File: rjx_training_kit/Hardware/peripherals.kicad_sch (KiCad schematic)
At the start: 72 parts, among them J4 LiPo_4.2V, J5 LiPo_4.2V, J6 CHG_OUT, J7 CAN_Bus, J8 CAN_Bus, Q2 BC817, Q3 BC817, Q4 BC808, Q5 BC817, SW1 SW_Push, U3 BQ24072RGT, U4 LIS3DH, U5 BQ27441-G1, U6 KCSA02-136, U7 TMP1075DGK, U8 MCP2562-E-SN

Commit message: [RJX]: Initial footprint assignment. This is subject to further review and analysis.
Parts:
- BZ1: footprint (none) -> Buzzer_Beeper:Buzzer_12x9.5RM7.6
- C10, C11, C12, C13, C14, C5, C6, C7, C8, C9: footprint (none) -> Capacitor_SMD:C_0603_1608Metric
- D2, D3, D4, D5: footprint (none) -> LED_SMD:LED_0603_1608Metric
- J4, J5: footprint (none) -> Connector_JST:JST_PH_B2B-PH-K_1x02_P2.00mm_Vertical
- J6, J7, J8, JP1, JP2, JP3, JP4: footprint (none) -> Connector_PinHeader_2.54mm:PinHeader_1x02_P2.54mm_Vertical
- R10, R11, R12, R14, R15, R16, R17, R19, R20, R21, R22, R23, R24, R25, R26, R27, R28, R29, R30, R31, R32, R33, R34, R35, R36, R37, R38, R39, R40, R6, R7, R8, R9: footprint (none) -> Resistor_SMD:R_0603_1608Metric
- R13, R18: footprint (none) -> Resistor_SMD:R_2512_6332Metric
- RV1: footprint (none) -> Potentiometer_THT:Potentiometer_Bourns_3296W_Vertical
- SW1: footprint (none) -> Button_Switch_THT:SW_PUSH_6mm
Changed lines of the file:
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@@
 			)
 		)
-		(property "Footprint" ""
+		(property "Footprint" "Resistor_SMD:R_0603_1608Metric"
 			(at 143.764 152.654 90)
 			(effects
@@
 			)
 		)
-		(property "Footprint" ""
+		(property "Footprint" "Capacitor_SMD:C_0603_1608Metric"
 			(at 186.9948 138.43 0)
 			(effects
@@
 			)
 		)
-		(property "Footprint" ""
+		(property "Footprint" "Resistor_SMD:R_0603_1608Metric"
 			(at 39.116 118.364 90)
 			(effects
@@
 			)
 		)
-		(property "Footprint" ""
+		(property "Footprint" "Resistor_SMD:R_0603_1608Metric"
 			(at 138.684 188.214 90)
 			(effects
@@
 			)
 		)
-		(property "Footprint" ""
+		(property "Footprint" "Connector_PinHeader_2.54mm:PinHeader_1x02_P2.54mm_Vertical"
 			(at 248.92 123.19 0)
 			(effects
@@
 			)
 		)
-		(property "Footprint" ""
+		(property "Footprint" "Resistor_SMD:R_0603_1608Metric"
 			(at 209.296 78.994 90)
 			(effects
@@
 			)
 		)
-		(property "Footprint" ""
+		(property "Footprint" "Resistor_SMD:R_0603_1608Metric"
 			(at 216.154 70.104 90)
 			(effects
@@
 			)
 		)
-		(property "Footprint" ""
+		(property "Footprint" "Capacitor_SMD:C_0603_1608Metric"
 			(at 148.2852 85.09 0)
 			(effects
@@
 			)
 		)
-		(property "Footprint" ""
+		(property "Footprint" "Resistor_SMD:R_0603_1608Metric"
 			(at 230.124 157.734 90)
 			(effects
@@
 			)
 		)
-		(property "Footprint" ""
+		(property "Footprint" "Capacitor_SMD:C_0603_1608Metric"
 			(at 103.8352 153.67 0)
 			(effects
@@
 			)
 		)
-		(property "Footprint" ""
+		(property "Footprint" "Resistor_SMD:R_0603_1608Metric"
 			(at 101.854 76.454 90)
 			(effects
@@
 			)
 		)
-		(property "Footprint" ""
+		(property "Footprint" "Resistor_SMD:R_0603_1608Metric"
 			(at 138.684 175.514 90)
 			(effects
@@
 			)
 		)
-		(property "Footprint" ""
+		(property "Footprint" "Resistor_SMD:R_0603_1608Metric"
 			(at 195.834 33.274 90)
 			(effects
@@
 			)
 		)
-		(property "Footprint" ""
+		(property "Footprint" "Resistor_SMD:R_0603_1608Metric"
 			(at 151.384 157.734 90)
 			(effects
@@
 			)
 		)
-		(property "Footprint" ""
+		(property "Footprint" "Capacitor_SMD:C_0603_1608Metric"
 			(at 126.6952 44.45 0)
 			(effects
@@
 			)
 		)
-		(property "Footprint" ""
+		(property "Footprint" "Resistor_SMD:R_0603_1608Metric"
 			(at 28.194 164.084 90)
 			(effects
@@
 			)
 		)
-		(property "Footprint" ""
+		(property "Footprint" "Connector_PinHeader_2.54mm:PinHeader_1x02_P2.54mm_Vertical"
 			(at 259.08 123.19 0)
 			(effects
@@
 			)
 		)
-		(property "Footprint" ""
+		(property "Footprint" "Resistor_SMD:R_0603_1608Metric"
 			(at 205.486 33.274 90)
 			(effects
@@
 			)
 		)
-		(property "Footprint" ""
+		(property "Footprint" "Connector_PinHeader_2.54mm:PinHeader_1x02_P2.54mm_Vertical"
 			(at 20.32 81.28 0)
 			(effects
@@
 			)
 		)
-		(property "Footprint" ""
+		(property "Footprint" "Resistor_SMD:R_0603_1608Metric"
 			(at 230.886 48.006 90)
 			(effects
@@
 			)
 		)
-		(property "Footprint" ""
+		(property "Footprint" "LED_SMD:LED_0603_1608Metric"
 			(at 200.66 44.45 0)
 			(effects
@@
 			)
 		)
-		(property "Footprint" ""
+		(property "Footprint" "Connector_JST:JST_PH_B2B-PH-K_1x02_P2.00mm_Vertical"
 			(at 34.29 39.37 0)
 			(effects
@@
 			)
 		)
-		(property "Footprint" ""
+		(property "Footprint" "Capacitor_SMD:C_0603_1608Metric"
 			(at 83.5152 87.63 0)
 			(effects
@@
 			)
 		)
-		(property "Footprint" ""
+		(property "Footprint" "Resistor_SMD:R_0603_1608Metric"
 			(at 138.684 180.594 90)
 			(effects
@@
 			)
 		)
-		(property "Footprint" ""
+		(property "Footprint" "Potentiometer_THT:Potentiometer_Bourns_3296W_Vertical"
 			(at 240.03 46.99 0)
 			(effects
@@
 			)
 		)
-		(property "Footprint" ""
+		(property "Footprint" "Resistor_SMD:R_0603_1608Metric"
 			(at 138.684 172.974 90)
 			(effects
@@
 			)
 		)
-		(property "Footprint" ""
+		(property "Footprint" "Resistor_SMD:R_2512_6332Metric"
 			(at 119.634 101.854 90)
 			(effects
@@
 			)
 		)
-		(property "Footprint" ""
+		(property "Footprint" "Capacitor_SMD:C_0603_1608Metric"
 			(at 186.9948 111.76 0)
 			(effects
@@
 			)
 		)
-		(property "Footprint" ""
+		(property "Footprint" "Resistor_SMD:R_2512_6332Metric"
 			(at 91.694 100.584 90)
 			(effects
@@
 			)
 		)
-		(property "Footprint" ""
+		(property "Footprint" "Resistor_SMD:R_0603_1608Metric"
 			(at 30.226 118.364 90)
 			(effects
@@
 			)
 		)
-		(property "Footprint" ""
+		(property "Footprint" "Resistor_SMD:R_0603_1608Metric"
 			(at 138.684 185.674 90)
 			(effects
@@
 			)
 		)
-		(property "Footprint" ""
+		(property "Footprint" "Resistor_SMD:R_0603_1608Metric"
 			(at 61.976 35.814 90)
 			(effects
@@
 			)
 		)
-		(property "Footprint" ""
+		(property "Footprint" "Capacitor_SMD:C_0603_1608Metric"
 			(at 115.2652 153.67 0)
 			(effects
@@
 			)
 		)
-		(property "Footprint" ""
+		(property "Footprint" "Connector_PinHeader_2.54mm:PinHeader_1x02_P2.54mm_Vertical"
 			(at 154.94 140.97 0)
 			(effects
@@
 			)
 		)
-		(property "Footprint" ""
+		(property "Footprint" "Resistor_SMD:R_0603_1608Metric"
 			(at 138.684 183.134 90)
 			(effects
@@
 			)
 		)
-		(property "Footprint" ""
+		(property "Footprint" "Resistor_SMD:R_0603_1608Metric"
 			(at 227.076 131.064 90)
 			(effects
@@
 			)
 		)
-		(property "Footprint" ""
+		(property "Footprint" "Resistor_SMD:R_0603_1608Metric"
 			(at 21.336 118.364 90)
 			(effects
@@
 			)
 		)
-		(property "Footprint" ""
+		(property "Footprint" "Resistor_SMD:R_0603_1608Metric"
 			(at 75.946 115.824 90)
 			(effects
@@
 			)
 		)
-		(property "Footprint" ""
+		(property "Footprint" "Connector_PinHeader_2.54mm:PinHeader_1x02_P2.54mm_Vertical"
 			(at 240.03 31.75 0)
 			(effects
@@
 			)
 		)
-		(property "Footprint" ""
+		(property "Footprint" "Resistor_SMD:R_0603_1608Metric"
 			(at 99.314 115.824 90)
 			(effects
@@
 			)
 		)
-		(property "Footprint" ""
+		(property "Footprint" "Resistor_SMD:R_0603_1608Metric"
 			(at 127.254 92.964 90)
 			(effects
@@
 			)
 		)
-		(property "Footprint" ""
+		(property "Footprint" "LED_SMD:LED_0603_1608Metric"
 			(at 111.76 85.09 0)
 			(effects
@@
 			)
 		)
-		(property "Footprint" ""
+		(property "Footprint" "Buzzer_Beeper:Buzzer_12x9.5RM7.6"
 			(at 45.085 152.4 90)
 			(effects
@@
 			)
 		)
-		(property "Footprint" ""
+		(property "Footprint" "Capacitor_SMD:C_0603_1608Metric"
 			(at 74.6252 43.18 0)
 			(effects
@@
 			)
 		)
-		(property "Footprint" ""
+		(property "Footprint" "Capacitor_SMD:C_0603_1608Metric"
 			(at 83.5152 116.84 0)
 			(effects
@@
 			)
 		)
-		(property "Footprint" ""
+		(property "Footprint" "Resistor_SMD:R_0603_1608Metric"
 			(at 138.176 40.894 90)
 			(effects
@@
 			)
 		)
-		(property "Footprint" ""
+		(property "Footprint" "LED_SMD:LED_0603_1608Metric"
 			(at 133.35 101.6 0)
 			(effects
@@
 			)
 		)
-		(property "Footprint" ""
+		(property "Footprint" "Resistor_SMD:R_0603_1608Metric"
 			(at 108.204 115.824 90)
 			(effects
@@
 			)
 		)
-		(property "Footprint" ""
+		(property "Footprint" "Resistor_SMD:R_0603_1608Metric"
 			(at 138.684 190.754 90)
 			(effects
@@
 			)
 		)
-		(property "Footprint" ""
+		(property "Footprint" "Button_Switch_THT:SW_PUSH_6mm"
 			(at 157.48 43.18 0)
 			(effects
@@
 			)
 		)
-		(property "Footprint" ""
+		(property "Footprint" "Resistor_SMD:R_0603_1608Metric"
 			(at 230.124 162.814 90)
 			(effects
@@
 			)
 		)
-		(property "Footprint" ""
+		(property "Footprint" "Capacitor_SMD:C_0603_1608Metric"
 			(at 21.2852 96.52 0)
 			(effects
@@
 			)
 		)
-		(property "Footprint" ""
+		(property "Footprint" "Resistor_SMD:R_0603_1608Metric"
 			(at 230.124 160.274 90)
 			(effects
@@
 			)
 		)
-		(property "Footprint" ""
+		(property "Footprint" "Resistor_SMD:R_0603_1608Metric"
 			(at 61.976 45.974 90)
 			(effects
@@
 			)
 		)
-		(property "Footprint" ""
+		(property "Footprint" "Resistor_SMD:R_0603_1608Metric"
 			(at 101.854 84.074 90)
 			(effects
@@
 			)
 		)
-		(property "Footprint" ""
+		(property "Footprint" "Connector_PinHeader_2.54mm:PinHeader_1x02_P2.54mm_Vertical"
 			(at 226.06 119.38 0)
 			(effects
@@
 			)
 		)
-		(property "Footprint" ""
+		(property "Footprint" "LED_SMD:LED_0603_1608Metric"
 			(at 111.76 77.47 0)
 			(effects
@@
 			)
 		)
-		(property "Footprint" ""
+		(property "Footprint" "Connector_PinHeader_2.54mm:PinHeader_1x02_P2.54mm_Vertical"
 			(at 45.72 36.83 0)
 			(effects
@@
 			)
 		)
-		(property "Footprint" ""
+		(property "Footprint" "Resistor_SMD:R_0603_1608Metric"
 			(at 138.684 178.054 90)
 			(effects
@@
 			)
 		)
-		(property "Footprint" ""
+		(property "Footprint" "Resistor_SMD:R_0603_1608Metric"
 			(at 161.544 32.004 90)
 			(effects
@@
 			)
 		)
-		(property "Footprint" ""
+		(property "Footprint" "Connector_JST:JST_PH_B2B-PH-K_1x02_P2.00mm_Vertical"
 			(at 22.86 36.83 0)
 			(effects

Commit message: [RJX]: Replaced the vertical footprint for the JST connector with a horizontal one.
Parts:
- J4, J5: footprint Connector_JST:JST_PH_B2B-PH-K_1x02_P2.00mm_Vertical -> Connector_JST:JST_PH_S2B-PH-K_1x02_P2.00mm_Horizontal
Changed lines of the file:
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@@
 			)
 		)
-		(property "Footprint" "Connector_JST:JST_PH_B2B-PH-K_1x02_P2.00mm_Vertical"
+		(property "Footprint" "Connector_JST:JST_PH_S2B-PH-K_1x02_P2.00mm_Horizontal"
 			(at 34.29 39.37 0)
 			(effects
@@
 			)
 		)
-		(property "Footprint" "Connector_JST:JST_PH_B2B-PH-K_1x02_P2.00mm_Vertical"
+		(property "Footprint" "Connector_JST:JST_PH_S2B-PH-K_1x02_P2.00mm_Horizontal"
 			(at 22.86 36.83 0)
 			(effects

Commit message: [RJX]: Schematic, Netlist, and PCB update. Replaced 2-pin crystal with 4-pin passive crystal.
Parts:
- DS1: footprint Display:WC1602A -> Connector_PinSocket_2.54mm:PinSocket_1x16_P2.54mm_Vertical
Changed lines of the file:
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@@
 			)
 		)
-		(property "Footprint" "Display:WC1602A"
+		(property "Footprint" "Connector_PinSocket_2.54mm:PinSocket_1x16_P2.54mm_Vertical"
 			(at 255.27 91.44 0)
 			(effects

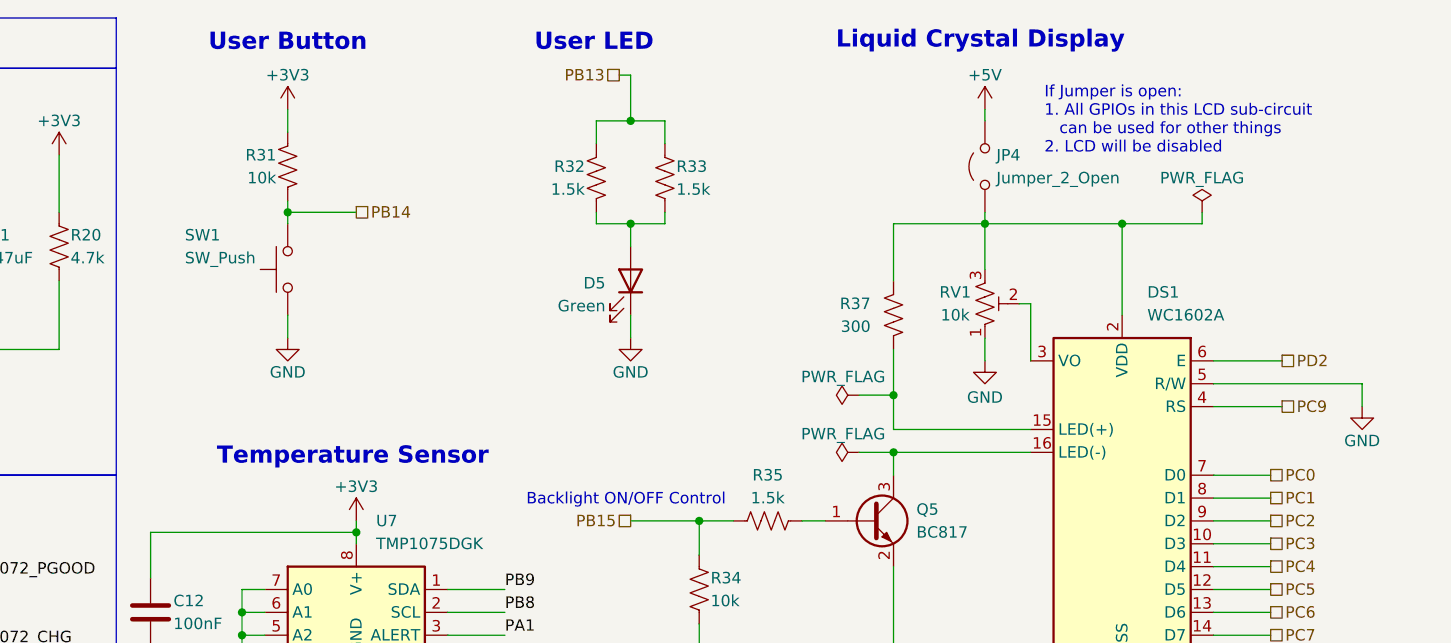
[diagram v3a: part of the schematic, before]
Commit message: [RJX]: Modified the schematic to account for different types of LCDs (some have current-limiting resistors, others don't). Also changed Links.md to an inner README.md file
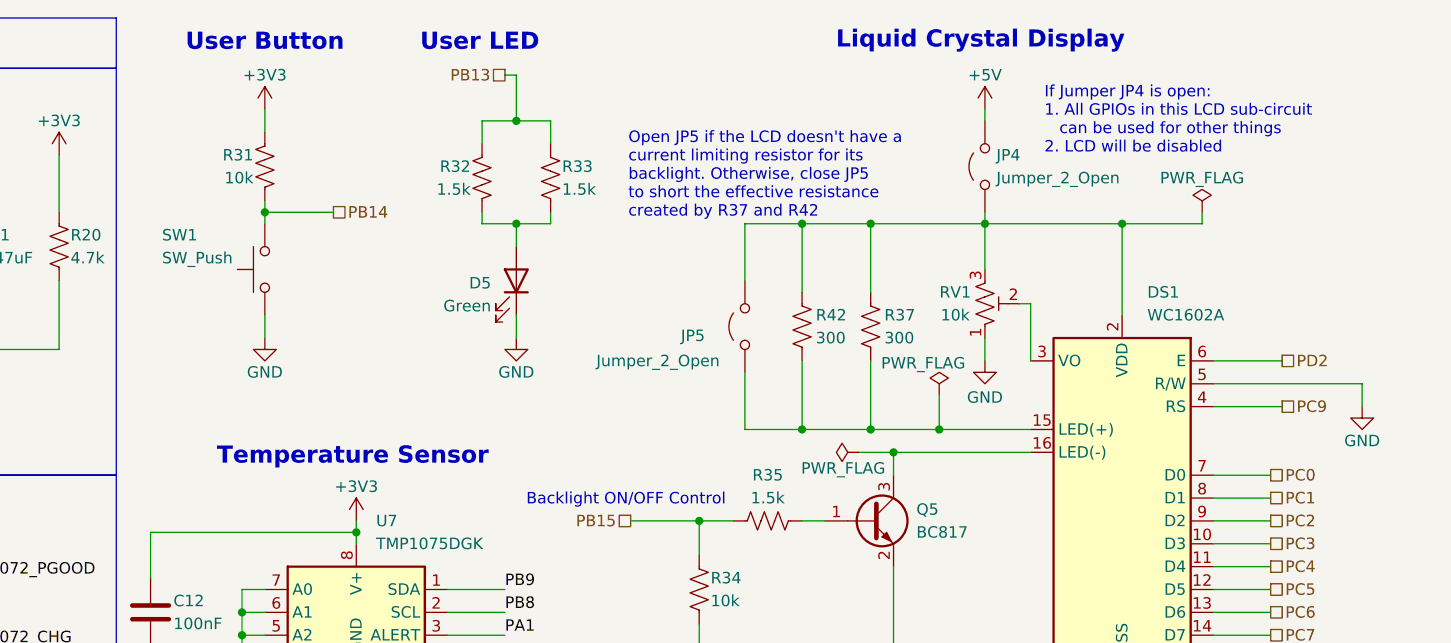
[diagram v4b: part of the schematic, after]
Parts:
- added JP5: Jumper_2_Open, Connector_PinHeader_2.54mm:PinHeader_1x02_P2.54mm_Vertical, symbol Jumper:Jumper_2_Open
- added R42: 300, Resistor_SMD:R_0603_1608Metric, symbol Device:R_US
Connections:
- net at DS1.15 (LED(+)), R37.1: now also JP5.1 (A), R42.1
- net at DS1.2 (VDD), JP4.1 (A), R37.2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: now also JP5.2 (B), R42.2
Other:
- note added: "If Jumper JP4 is open: 1. All GPIOs in this LCD sub-circuit can be used for other things 2. LCD will be disabled"
- note added: "Open JP5 if the LCD doesn't have a current limiting resistor for its backlight. Otherwise, close JP5 to short the effective resistance created by R37 and R42"
- note removed: "If Jumper is open: 1. All GPIOs in this LCD sub-circuit can be used for other things 2. LCD will be disabled"
- company: (none) -> RJX Embedded
- moved on the sheet: D5, R31, R32, R33, R37, SW1
